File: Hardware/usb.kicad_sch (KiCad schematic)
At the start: 4 parts, among them J3 USB_C_Receptacle_USB2.0_16P, U2 USBLC6-2SC6

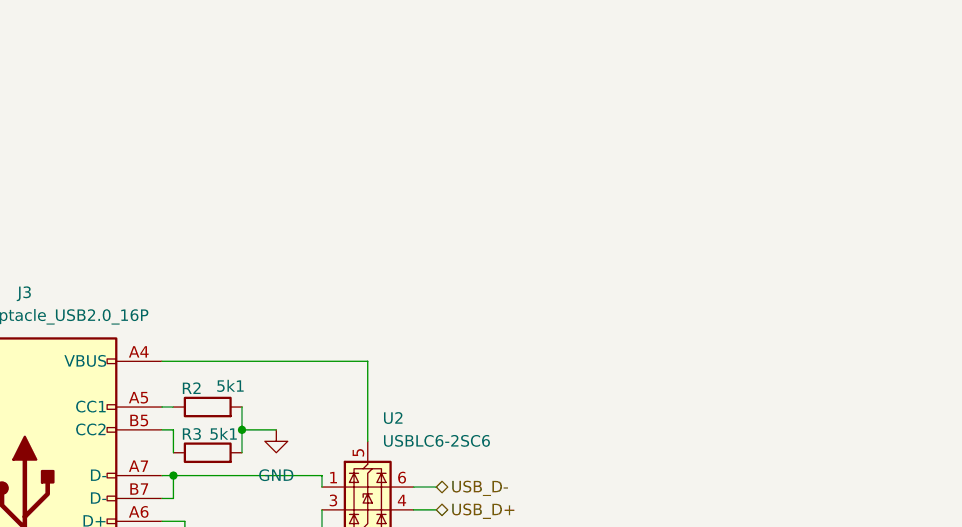
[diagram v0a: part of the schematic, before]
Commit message: [Alimentation de la Carte]: Source provient de l'USB L'USB fournit une tension d'alimentation de 5V, et pour l'exploiter j'utilise un régulateur de tension stable en 3.3V. Le régulateur utilisé est le MIC5365-3.3YD5S5. Pour vérifier si la carte est bien alimenter j'utilise une led de controle D1.
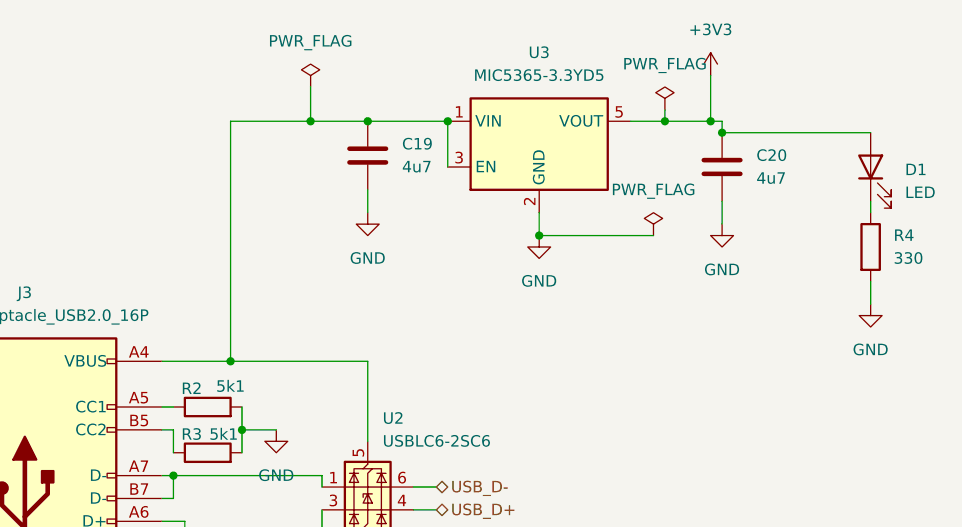
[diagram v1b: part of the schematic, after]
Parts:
- added C19, C20: 4u7, symbol Device:C
- added D1: LED, symbol Device:LED
- added R4: 330, symbol Device:R
- added U3: MIC5365-3.3YD5, Package_TO_SOT_SMD:TSOT-23-5, symbol Regulator_Linear:MIC5365-3.3YD5
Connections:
- net GND: now also C19.2, C20.2, R4.2, U3.2 (GND)
- net at J3.A4 (VBUS), J3.A9 (VBUS), J3.B4 (VBUS)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: now also C19.1, U3.1 (VIN), U3.3 (EN)
- new net: D1.1 (K), R4.1
- new net +3V3: C20.1, D1.2 (A), U3.5 (VOUT)

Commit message: [Realisation] : Regulateur de Tension, Capteur BME280, Buzzer, MQ2 et Leds indicateurs.
Dans cette phase, j'ai réalisé les montages suivantes ;
Regulateur de Tension : La tension d'alimentation du système vient de
l'USB, donc en utilisant un regulateur de tension, on parvient à
abaisser la tension à 3.3V
Capteur BME280 : Le montage est réalisé comme recommandé par le
fabricant Bosch. En y précisant les résistance pull up pour le protocol
I2C.
Buzzer : Le buzzer va servir d'alerte en raisonnant.
Pour ce montage on utilise un transistor NPN pour amplifier le courant.
MQ2 : Pour ce capteur, on utilise des éléments traversant et de ce fait,
on va juste souder le composant à la carte.
Led Indicateurs : ces indicateurs vont servir de visuel pour juger le
niveau de la temperature.
D1 : Pour indiquer que la carte est sous tension
D2 : Pour indiquer que la temperature est < 20°C
D3 : Pour indiquer que la temperature est > 20°C et < 30°C
D4 : Pour indiquer que la temperature est > 30°C
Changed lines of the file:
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@@
-	)
-	(junction
-		(at 132.08 29.21)
-		(diameter 0)
-		(color 0 0 0 0)
 	)
 	(junction
@@
 	(wire
 		(pts
-			(xy 132.08 27.94) (xy 132.08 29.21)
-		)
-		(stroke
-			(width 0)
-			(type default)
-		)
-	)
-	(wire
-		(pts
 			(xy 99.06 29.21) (xy 107.95 29.21)
 		)
@@
 	(wire
 		(pts
-			(xy 128.27 29.21) (xy 132.08 29.21)
-		)
-		(stroke
-			(width 0)
-			(type default)
-		)
-	)
-	(wire
-		(pts
 			(xy 92.71 29.21) (xy 83.82 29.21)
 		)
@@
 	(wire
 		(pts
-			(xy 132.08 29.21) (xy 137.16 29.21)
+			(xy 128.27 29.21) (xy 137.16 29.21)
 		)
 		(stroke
@@
 					(unit 1)
 				)
-			)
-		)
-	)
-	(symbol
-		(lib_id "power:PWR_FLAG")
-		(at 132.08 27.94 0)
-		(unit 1)
-		(exclude_from_sim no)
-		(in_bom yes)
-		(on_board yes)
-		(dnp no)
-		(fields_autoplaced yes)
-		(property "Reference" "#FLG02"
-			(at 132.08 26.035 0)
-			(effects
-				(font
-					(size 1.27 1.27)
-				)
-				(hide yes)
-			)
-		)
-		(property "Value" "PWR_FLAG"
-			(at 132.08 22.86 0)
-			(effects
-				(font
-					(size 1.27 1.27)
-				)
-			)
-		)
-		(property "Footprint" ""
-			(at 132.08 27.94 0)
-			(effects
-				(font
-					(size 1.27 1.27)
-				)
-				(hide yes)
-			)
-		)
-		(property "Datasheet" "~"
-			(at 132.08 27.94 0)
-			(effects
-				(font
-					(size 1.27 1.27)
-				)
-				(hide yes)
-			)
-		)
-		(property "Description" "Special symbol for telling ERC where power comes from"
-			(at 132.08 27.94 0)
-			(effects
-				(font
-					(size 1.27 1.27)
-				)
-				(hide yes)
-			)
-		)
-		(pin "1"
-		)
-		(instances
-			(project ""
-				(path "/ba4846b8-7c71-441f-b11b-b34cbea60d05/f91aa170-a53f-4636-962a-1e68ecfd96a0"
-					(reference "#FLG02")
-					(unit 1)
-				)

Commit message: [EXECUTION ERC] : Le check électrique a bien marché sauf une erreur persistante sur VLXSMPS ce qui est un défaut du symbole créé et non du montage de découplage proposé par ST Microelectronics
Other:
- note added: "LED TO CHECK IF THE BOARD IS POWERED"
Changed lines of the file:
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@@
 	(generator_version "9.0")
 	(paper "A4")
+	(text "LED TO CHECK IF THE BOARD IS POWERED"
+		(exclude_from_sim no)
+		(at 183.642 35.306 0)
+		(effects
+			(font
+				(size 1.27 1.27)
+			)
+		)
+	)
 	(junction
 		(at 99.06 29.21)

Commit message: [FOOTPRINT ASSIGNMENT] : Ajout des footprints à chaque élément
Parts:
- C19, C20: footprint (none) -> Capacitor_SMD:C_0603_1608Metric
- D1: footprint (none) -> LED_SMD:LED_0402_1005Metric
- J3: footprint (none) -> Connector_USB:USB_C_Receptacle_GCT_USB4105-xx-A_16P_TopMnt_Horizontal
- R2, R3, R4: footprint (none) -> Resistor_SMD:R_0402_1005Metric
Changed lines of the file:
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@@
 			)
 		)
-		(property "Footprint" ""
+		(property "Footprint" "Capacitor_SMD:C_0603_1608Metric"
 			(at 100.0252 36.83 0)
 			(effects
@@
 			)
 		)
-		(property "Footprint" ""
+		(property "Footprint" "Capacitor_SMD:C_0603_1608Metric"
 			(at 139.3952 38.1 0)
 			(effects
@@
 			)
 		)
-		(property "Footprint" ""
+		(property "Footprint" "Resistor_SMD:R_0402_1005Metric"
 			(at 81.28 67.818 90)
 			(effects
@@
 			)
 		)
-		(property "Footprint" ""
+		(property "Footprint" "LED_SMD:LED_0402_1005Metric"
 			(at 154.94 34.29 0)
 			(effects
@@
 			)
 		)
-		(property "Footprint" ""
+		(property "Footprint" "Resistor_SMD:R_0402_1005Metric"
 			(at 153.162 43.18 90)
 			(effects
@@
 			)
 		)
-		(property "Footprint" ""
+		(property "Footprint" "Resistor_SMD:R_0402_1005Metric"
 			(at 81.28 62.738 90)
 			(effects
@@
 			)
 		)
-		(property "Footprint" ""
+		(property "Footprint" "Connector_USB:USB_C_Receptacle_GCT_USB4105-xx-A_16P_TopMnt_Horizontal"
 			(at 64.77 71.12 0)
 			(effects

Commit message: [FOOTPRINT ASSIGNMENT] : J'ai ajouté le +5V flag de l'USB, j'ai ajouté des labels pour avoir un netclass plus consistent
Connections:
- net +5V: now reaches C19.1, J3.A4 (VBUS), J3.A9 (VBUS), J3.B4 (VBUS), J3.B9 (VBUS), U2.5 (VBUS), U3.1 (VIN), U3.3 (EN)
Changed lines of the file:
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@@
+	)
+	(junction
+		(at 91.44 55.88)
+		(diameter 0)
+		(color 0 0 0 0)
 	)
 	(junction
@@
 	(wire
 		(pts
+			(xy 91.44 55.88) (xy 83.82 55.88)
+		)
+		(stroke
+			(width 0)
+			(type default)
+		)
+	)
+	(wire
+		(pts
 			(xy 92.71 29.21) (xy 83.82 29.21)
 		)
@@
 	(wire
 		(pts
+			(xy 91.44 54.61) (xy 91.44 55.88)
+		)
+		(stroke
+			(width 0)
+			(type default)
+		)
+	)
+	(wire
+		(pts
 			(xy 154.94 30.48) (xy 138.43 30.48)
 		)
@@
 	(wire
 		(pts
-			(xy 99.06 55.88) (xy 83.82 55.88)
+			(xy 99.06 55.88) (xy 91.44 55.88)
 		)
 		(stroke
@@
 					(unit 1)
 				)
+			)
+		)
+	)
+	(symbol
+		(lib_id "power:+5V")
+		(at 91.44 54.61 0)
+		(unit 1)
+		(exclude_from_sim no)
+		(in_bom yes)
+		(on_board yes)
+		(dnp no)
+		(fields_autoplaced yes)
+		(property "Reference" "#PWR045"
+			(at 91.44 58.42 0)
+			(effects
+				(font
+					(size 1.27 1.27)
+				)
+				(hide yes)
+			)
+		)
+		(property "Value" "+5V"
+			(at 91.44 49.53 0)
+			(effects
+				(font
+					(size 1.27 1.27)
+				)
+			)
+		)
+		(property "Footprint" ""
+			(at 91.44 54.61 0)
+			(effects
+				(font
+					(size 1.27 1.27)
+				)
+				(hide yes)
+			)
+		)
+		(property "Datasheet" ""
+			(at 91.44 54.61 0)
+			(effects
+				(font
+					(size 1.27 1.27)
+				)
+				(hide yes)
+			)
+		)
+		(property "Description" "Power symbol creates a global label with name \"+5V\""
+			(at 91.44 54.61 0)
+			(effects
+				(font
+					(size 1.27 1.27)
+				)
+				(hide yes)
+			)
+		)
+		(pin "1"
+		)
+		(instances
+			(project ""
+				(path "/ba4846b8-7c71-441f-b11b-b34cbea60d05/f91aa170-a53f-4636-962a-1e68ecfd96a0"
+					(reference "#PWR045")
+					(unit 1)
+				)

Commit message: [PLACEMENT DES COMPOSANT ET DIMENSIONNEMENT] : Avant de désigner le type de signal à chaque couche et commencer le routage, j'ai d'abord commencer par organiser les composants selon la schématique et comment j'aimerais avoir le produit finale
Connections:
- net D-: now reaches J3.A7 (D-), J3.B7 (D-), U2.1 (I/O1)
- net D+: now reaches J3.A6 (D+), J3.B6 (D+), U2.3 (I/O2)
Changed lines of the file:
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@@
+		)
+	)
+	(label "D-"
+		(at 85.09 68.58 0)
+		(effects
+			(font
+				(size 1.27 1.27)
+			)
+			(justify left bottom)
+		)
+	)
+	(label "D+"
+		(at 85.09 76.2 0)
+		(effects
+			(font
+				(size 1.27 1.27)
+			)
+			(justify left bottom)
 		)
 	)
@@
 		(on_board yes)
 		(dnp no)
-		(fields_autoplaced yes)
 		(property "Reference" "#PWR029"
 			(at 88.9 69.85 0)
@@
 		)
 		(property "Value" "GND"
-			(at 88.9 68.58 0)
-			(effects
-				(font
+			(at 92.202 63.5 0)
+			(effects
+				(font

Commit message: [Bill of Materials(BOM)]: Remplissage des informations tels que : manufacturer part number, manufacturer et la documentation du composant concerné. le BOM sera envoyé avec le fichier Geber au fabricant de PCB
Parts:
- C19, C20: Manufacturer (none) -> KYOCERA AVX; Manufacturer Part Number (none) -> 0603YD475MAT2A
- D1: Manufacturer (none) -> Wurth Elektronik; Manufacturer Part Number (none) -> 150040RS73240
- J3: Manufacturer (none) -> GCT; Manufacturer Part Number (none) -> USB4105-GF-A
- R2, R3: Manufacturer (none) -> YAGEO; Manufacturer Part Number (none) -> RC0402BR-075K1L
- R4: value 330 -> 220; Manufacturer (none) -> YAGEO; Manufacturer Part Number (none) -> RC0402FR-07221RL
- U2: Manufacturer (none) -> STMicroelectronics; Manufacturer Part Number (none) -> USBLC6-2SC6
- U3: Manufacturer (none) -> Microchip Technology; Manufacturer Part Number (none) -> MIC5365-3.3YD5-TR
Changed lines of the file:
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@@
 			)
 		)
-		(property "Datasheet" "~"
+		(property "Datasheet" "https://datasheets.kyocera-avx.com/cx5r.pdf"
 			(at 99.06 33.02 0)
 			(effects
@@
 		)
 		(property "Description" "Unpolarized capacitor"
+			(at 99.06 33.02 0)
+			(effects
+				(font
+					(size 1.27 1.27)
+				)
+				(hide yes)
+			)
+		)
+		(property "Manufacturer" "KYOCERA AVX"
+			(at 99.06 33.02 0)
+			(effects
+				(font
+					(size 1.27 1.27)
+				)
+				(hide yes)
+			)
+		)
+		(property "Manufacturer Part Number" "0603YD475MAT2A"
 			(at 99.06 33.02 0)
 			(effects
@@
 			)
 		)
-		(property "Datasheet" "~"
+		(property "Datasheet" "https://datasheets.kyocera-avx.com/cx5r.pdf"
 			(at 138.43 34.29 0)
 			(effects
@@
 		)
 		(property "Description" "Unpolarized capacitor"
+			(at 138.43 34.29 0)
+			(effects
+				(font
+					(size 1.27 1.27)
+				)
+				(hide yes)
+			)
+		)
+		(property "Manufacturer" "KYOCERA AVX"
+			(at 138.43 34.29 0)
+			(effects
+				(font
+					(size 1.27 1.27)
+				)
+				(hide yes)
+			)
+		)
+		(property "Manufacturer Part Number" "0603YD475MAT2A"
 			(at 138.43 34.29 0)
 			(effects
@@
 			)
 		)
+		(property "Manufacturer" "Microchip Technology"
+			(at 118.11 31.75 0)
+			(effects
+				(font
+					(size 1.27 1.27)
+				)
+				(hide yes)
+			)
+		)
+		(property "Manufacturer Part Number" "MIC5365-3.3YD5-TR"
+			(at 118.11 31.75 0)
+			(effects
+				(font
+					(size 1.27 1.27)
+				)
+				(hide yes)
+			)
+		)
 		(pin "5"
 		)
@@
 			)
 		)
-		(property "Datasheet" "~"
+		(property "Datasheet" "https://www.mouser.fr/ProductDetail/YAGEO/RC0402BR-075K1L?qs=eP2BKZSCXI5z8A6ic6YLjQ%3D%3D"
 			(at 81.28 66.04 0)
 			(effects
@@
 		(property "Description" "Resistor"
 			(at 81.28 66.04 0)
+			(effects
+				(font
+					(size 1.27 1.27)
+				)
+				(hide yes)
+			)
+		)
+		(property "Manufacturer" "YAGEO"
+			(at 81.28 66.04 90)
+			(effects
+				(font
+					(size 1.27 1.27)
+				)
+				(hide yes)
+			)
+		)
+		(property "Manufacturer Part Number" "RC0402BR-075K1L"
+			(at 81.28 66.04 90)
 			(effects
 				(font
@@
 			)
 		)
-		(property "Datasheet" "~"
+		(property "Datasheet" "https://www.we-online.com/components/products/datasheet/150040RS73240.pdf"
 			(at 154.94 34.29 0)
 			(effects
@@
 		(property "Sim.Pins" "1=K 2=A"
 			(at 154.94 34.29 0)
+			(effects
+				(font
+					(size 1.27 1.27)
+				)
+				(hide yes)
+			)
+		)
+		(property "Manufacturer" "Wurth Elektronik"
+			(at 154.94 34.29 90)
+			(effects
+				(font
+					(size 1.27 1.27)
+				)
+				(hide yes)
+			)
+		)
+		(property "Manufacturer Part Number" "150040RS73240"
+			(at 154.94 34.29 90)
 			(effects
 				(font
@@
 			)
 		)
-		(property "Value" "330"
+		(property "Value" "220"
 			(at 157.48 44.4499 0)
 			(effects
@@
 			)
 		)
-		(property "Datasheet" "~"
+		(property "Datasheet" "https://www.mouser.com/catalog/specsheets/YAGEO_PYu_RC_Group_51_RoHS_L_12.pdf"
 			(at 154.94 43.18 0)
 			(effects
@@
 		)
 		(property "Description" "Resistor"
+			(at 154.94 43.18 0)
+			(effects
+				(font
+					(size 1.27 1.27)
+				)
+				(hide yes)
+			)
+		)
+		(property "Manufacturer" "YAGEO"
+			(at 154.94 43.18 0)
+			(effects
+				(font
+					(size 1.27 1.27)
+				)
+				(hide yes)
+			)
+		)
+		(property "Manufacturer Part Number" "RC0402FR-07221RL"
 			(at 154.94 43.18 0)
 			(effects
@@
 			)
 		)
+		(property "Manufacturer" "STMicroelectronics"
+			(at 99.06 69.85 0)
+			(effects
+				(font
+					(size 1.27 1.27)
+				)
+				(hide yes)
+			)
+		)
+		(property "Manufacturer Part Number" "USBLC6-2SC6"
+			(at 99.06 69.85 0)
+			(effects
+				(font
+					(size 1.27 1.27)
+				)
+				(hide yes)
+			)
+		)
 		(pin "2"
 		)
@@
 			)
 		)
-		(property "Datasheet" "~"
+		(property "Datasheet" "https://www.mouser.fr/ProductDetail/YAGEO/RC0402BR-075K1L?qs=eP2BKZSCXI5z8A6ic6YLjQ%3D%3D"
 			(at 81.28 60.96 0)
 			(effects
@@
 		(property "Description" "Resistor"
 			(at 81.28 60.96 0)
+			(effects
+				(font
+					(size 1.27 1.27)
+				)
+				(hide yes)
+			)
+		)
+		(property "Manufacturer" "YAGEO"
+			(at 81.28 60.96 90)
+			(effects
+				(font
+					(size 1.27 1.27)
+				)
+				(hide yes)
+			)
+		)
+		(property "Manufacturer Part Number" "RC0402BR-075K1L"
+			(at 81.28 60.96 90)
 			(effects
 				(font
@@
 			(at 60.96 71.12 0)
 			(effects
+				(font
+					(size 1.27 1.27)
+				)
+				(hide yes)
+			)
+		)
+		(property "Manufacturer" "GCT"
+			(at 60.96 71.12 0)
+			(effects
+				(font
+					(size 1.27 1.27)
+				)
+				(hide yes)
+			)
+		)
+		(property "Manufacturer Part Number" "USB4105-GF-A"
+			(at 60.96 71.12 0)
+			(effects

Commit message: [CORRECCTION DU PCB] : J'ai corrigé le PCB après avoir discuter avec le Fabricant PCB Way, j'ai corrigé le footprint de la capacité C14 avec ce qui correspond à ce qui est vendu par mouser electronics. Le bon footprint est 0402_1005. J'ai également corrigé le footprint des connecteurs 01x04 avec un footprint de 2.54mm. Avant c'était 1mm, du coup j'ai modifié le PCB. J'ai également modifier le placement des capacité et des inductances, plus proche du stm32.
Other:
- company: (none) -> PAR KAMDA JONATAN
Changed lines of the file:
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@@
 	(generator_version "9.0")
 	(paper "A4")
+	(title_block
+		(company "PAR KAMDA JONATAN")
+	)
 	(text "LED TO CHECK IF THE BOARD IS POWERED"
 		(exclude_from_sim no)
